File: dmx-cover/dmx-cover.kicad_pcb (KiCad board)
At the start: 2 copper layers, 66 x 18 mm, 7 parts

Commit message: Update to KiCad 7.0
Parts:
- H1: value MountingHole -> MountingHole_1mm; footprint V2_Mechanical:Mounting_Hole_1 -> V2_Mechanical:MountingHole_1mm
- H2, H3: value MountingHole_Pad -> MountingHole_2mm_Pad_5.2mm; footprint V2_Mechanical:Mounting_Hole_Pad_2-5.2 -> V2_Mechanical:Mounting_Hole_2mm_Pad_5.2mm
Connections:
- net /SHIELD renamed GND

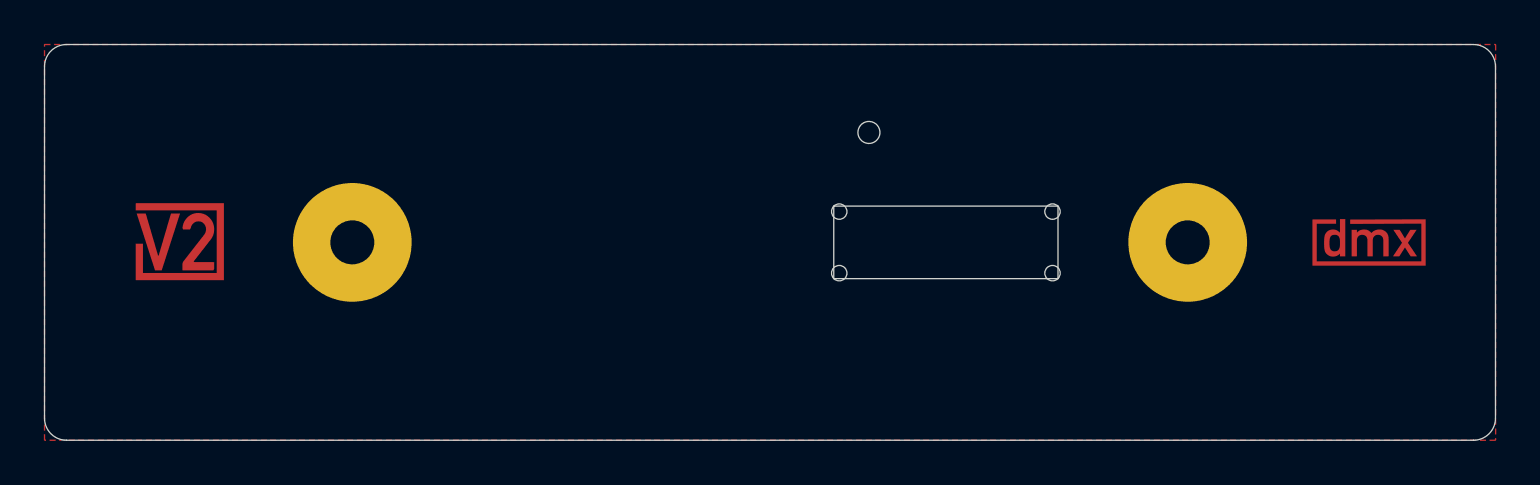
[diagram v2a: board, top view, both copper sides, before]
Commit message: Update TRS socket
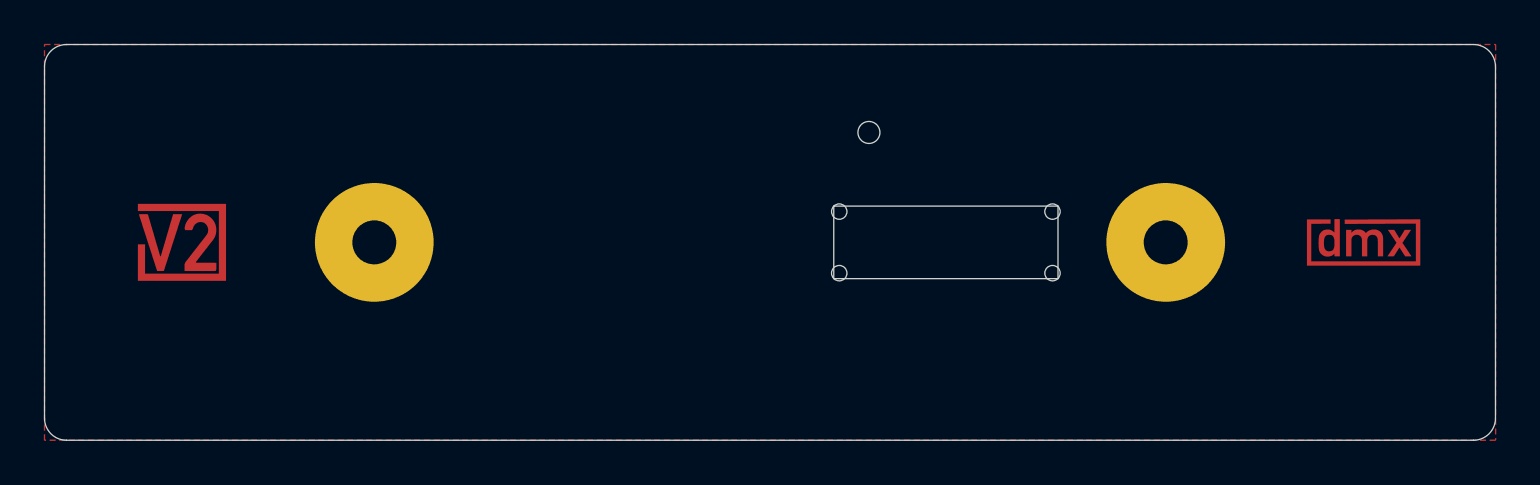
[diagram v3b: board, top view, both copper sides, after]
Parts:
- H2, H3: footprint V2_Mechanical:Mounting_Hole_2mm_Pad_5.2mm -> V2_Mechanical:MountingHole_2mm_Pad_5.2mm
- moved H2 1.00 mm to (168.0, 106.0)
- moved H3 1.00 mm to (132.0, 106.0)
- moved ICON2 0.25 mm to (177.0, 106.0)
